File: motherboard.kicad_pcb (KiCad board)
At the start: 2 copper layers, 90.2 x 95.9 mm, 94 parts, among them P1 CONN_02X08, U1 STM32F411-LQFP64, U10 74LS125, U11 74LS125, U12 74LS125, U13 74LS125, U14 PCA9517A, U15 PCA9517A, U16 74LS125, U17 74LS125, U2 STM32F411-LQFP64, U3 AP7313, U4 74LS00, U5 74LS125, U6 FM25V20A-G, U7 FM25V20A-G, U8 FM25V20A-G, U9 FM25V20A-G, Y1 32k, Y2 8M(16pF), Y3 32k, Y4 8M(16pF)

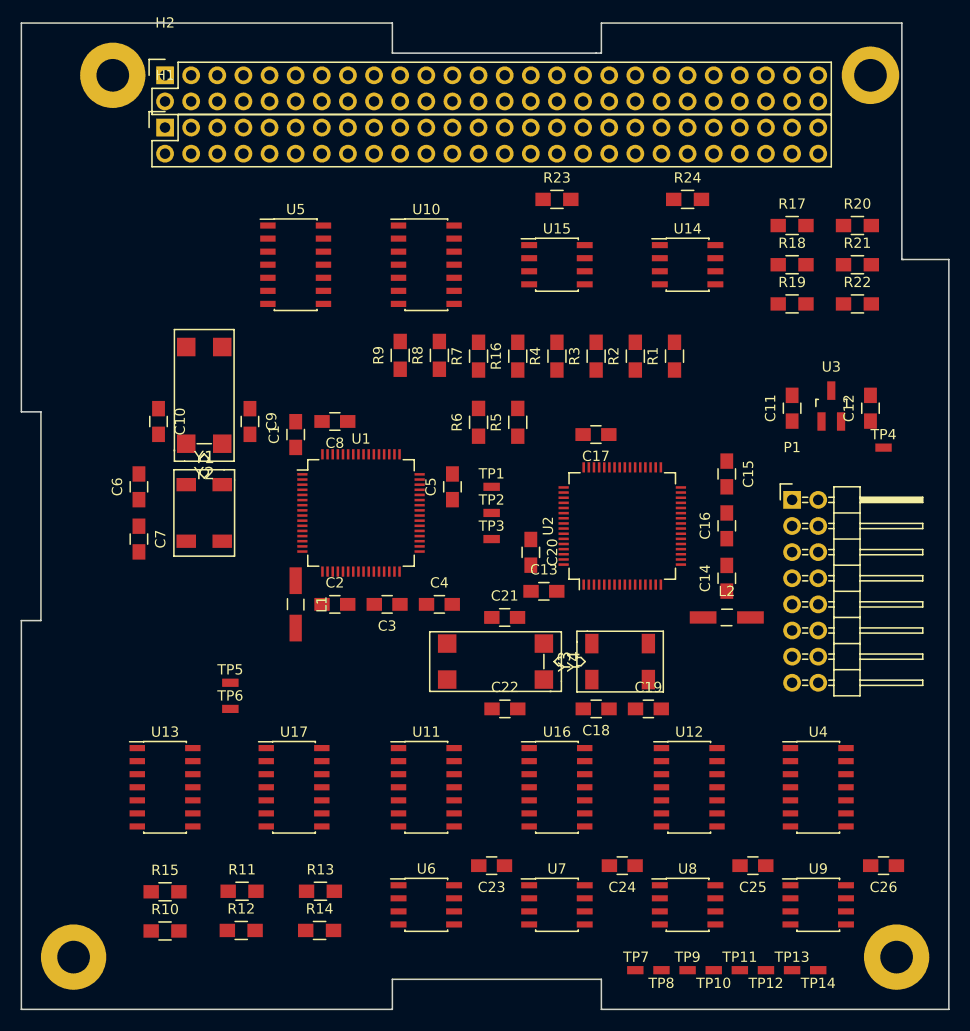
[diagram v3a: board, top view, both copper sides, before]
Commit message: Routed P1 High-speed signals
- Main UART
- Main I2C
- Mem SPI
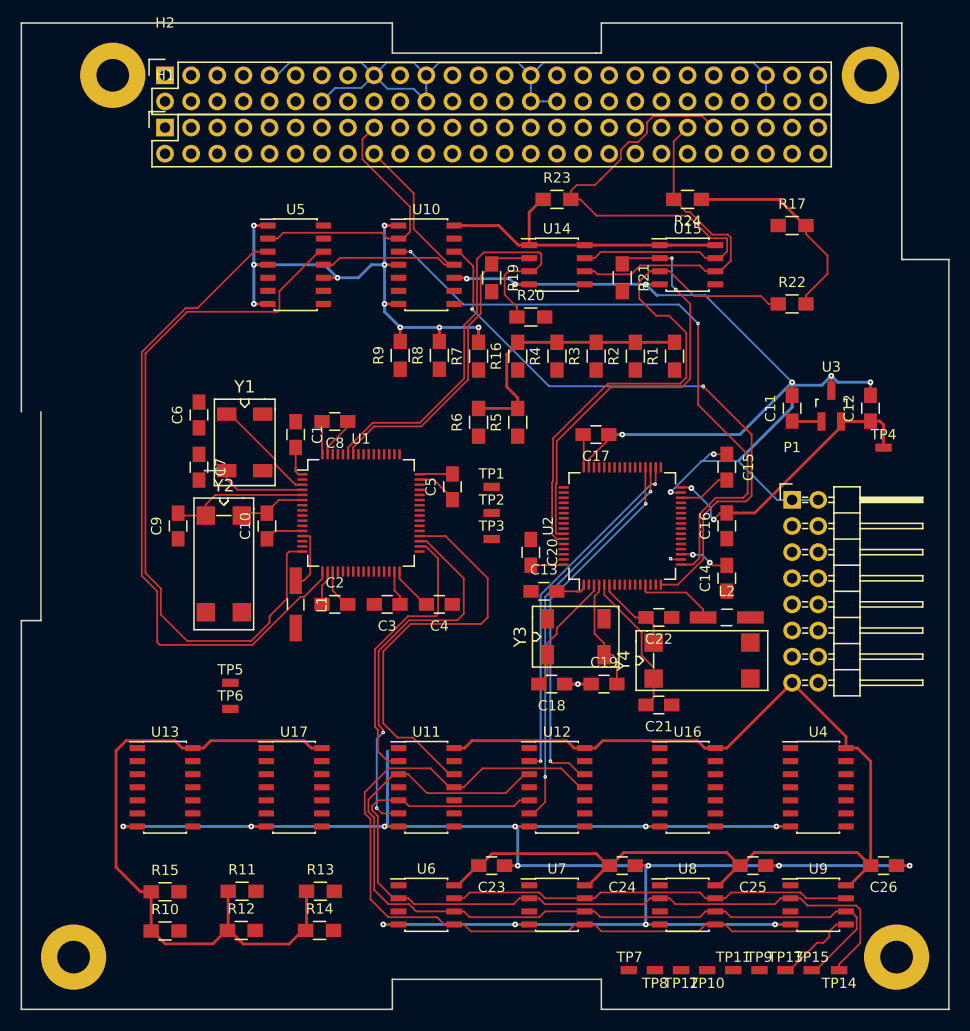
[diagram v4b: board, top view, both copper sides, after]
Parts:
- removed R18: 100K, Resistors_SMD:R_0805_HandSoldering
- added TP15: TP, motherboard:TP_0603, F.Cu at (189.9, 138.4)
- moved R20 33.0 mm to (162.6, 74.9)
- moved R19 29.3 mm to (158.8, 71.1), turned to 270 degrees
- moved R21 22.9 mm to (171.4, 71.1), turned to 270 degrees
- moved Y4 20.1 mm to (179.2, 108.3), turned to 0 degrees
- moved C22 17.4 mm to (175.0, 104.1), turned to 180 degrees
- moved C21 17.2 mm to (175.0, 112.6), turned to 180 degrees
- moved Y2 16.5 mm to (132.7, 98.9), turned to 270 degrees
- moved C10 14.6 mm to (136.9, 95.2), turned to 90 degrees
- moved U12 12.9 mm to (165.1, 120.7)
- moved U14 12.7 mm to (165.1, 69.8)
- moved U15 12.7 mm to (177.8, 69.8)
- moved U16 12.7 mm to (177.8, 120.7)
- moved C9 12.3 mm to (128.3, 95.2), turned to 90 degrees
- moved C6 9.11 mm to (130.3, 84.5)
- moved C7 9.11 mm to (130.3, 89.5)
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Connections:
- R15 pad 2: Net-(R15-Pad2) -> /MEM_NHOLD
- U11 pad 1: GND -> /NBUFEN_PRI
- U11 pad 11: /SYS_RESET -> /MEM_MOSI
- U11 pad 12: /SYS_RESET_P -> /MEM_MOSI_P
- U11 pad 2: /MEM_MISO -> /MEM_SCK_P
- U11 pad 3: /MEM_MISO_P -> /MEM_SCK
- U11 pad 4: /NBUFEN_PRI -> GND
- U11 pad 5: /MEM_SCK_P -> /MEM_MISO
- U11 pad 6: /MEM_SCK -> /MEM_MISO_P
- U11 pad 8: /MEM_MOSI -> /SYS_RESET
- U11 pad 9: /MEM_MOSI_P -> /SYS_RESET_P
- U12 pad 1: GND -> /NBUFEN_SEC
- U12 pad 11: /SYS_RESET -> /MEM_MOSI
- U12 pad 12: /SYS_RESET_S -> /MEM_MOSI_S
- U12 pad 2: /MEM_MISO -> /MEM_SCK_S
- U12 pad 3: /MEM_MISO_S -> /MEM_SCK
- U12 pad 4: /NBUFEN_SEC -> GND
- U12 pad 5: /MEM_SCK_S -> /MEM_MISO
- U12 pad 6: /MEM_SCK -> /MEM_MISO_S
- U12 pad 8: /MEM_MOSI -> /SYS_RESET
- U12 pad 9: /MEM_MOSI_S -> /SYS_RESET_S
- U6 pad 7: Net-(R15-Pad2) -> /MEM_NHOLD
- U7 pad 7: Net-(R15-Pad2) -> /MEM_NHOLD
- U8 pad 7: Net-(R15-Pad2) -> /MEM_NHOLD
- U9 pad 7: Net-(R15-Pad2) -> /MEM_NHOLD
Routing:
- net GND: track 0.00 -> 433.9 mm, vias 0 -> 35
- net +3V3: track 0.00 -> 275.9 mm
- net /MEM_MOSI: track 0.00 -> 91.1 mm
- net /MEM_SCK: track 0.00 -> 83.8 mm
- net /MEM_MISO: track 0.00 -> 79.8 mm
- net /RADIO_TX_P: track 0.00 -> 69.8 mm
- net /RADIO_RX_P: track 0.00 -> 64.7 mm
- net /RADIO_RX_S: track 0.00 -> 62.4 mm, vias 0 -> 2
- net /RADIO_TX_S: track 0.00 -> 60.0 mm, vias 0 -> 2
- net /SYS_SDA_S: track 0.00 -> 53.7 mm
- net /SYS_SCL: track 0.00 -> 52.1 mm
- net /SYS_SDA_P: track 0.00 -> 43.0 mm
- net /VDD_S: track 0.00 -> 43.0 mm, vias 0 -> 4
- net /SYS_SCL_S: track 0.00 -> 42.8 mm, vias 0 -> 2
- net /MEM_NHOLD: track 0.00 -> 40.5 mm
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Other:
- outline, holes or cut-outs redrawn
- net class Power: clearance 0.2286 -> 0.2794; trace_width 0.2286 -> 0.2794; via_dia 0.508 -> 0.5588

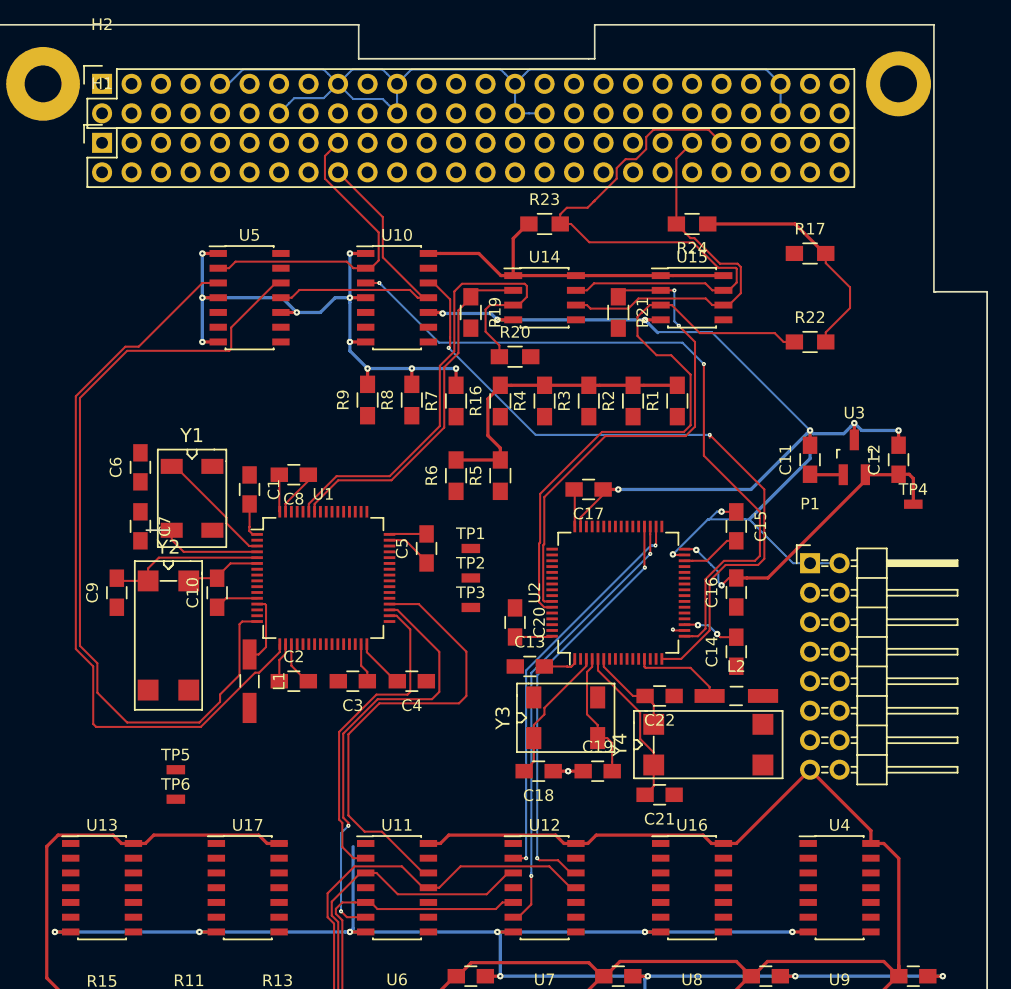
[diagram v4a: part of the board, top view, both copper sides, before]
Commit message: Much more routing completed.
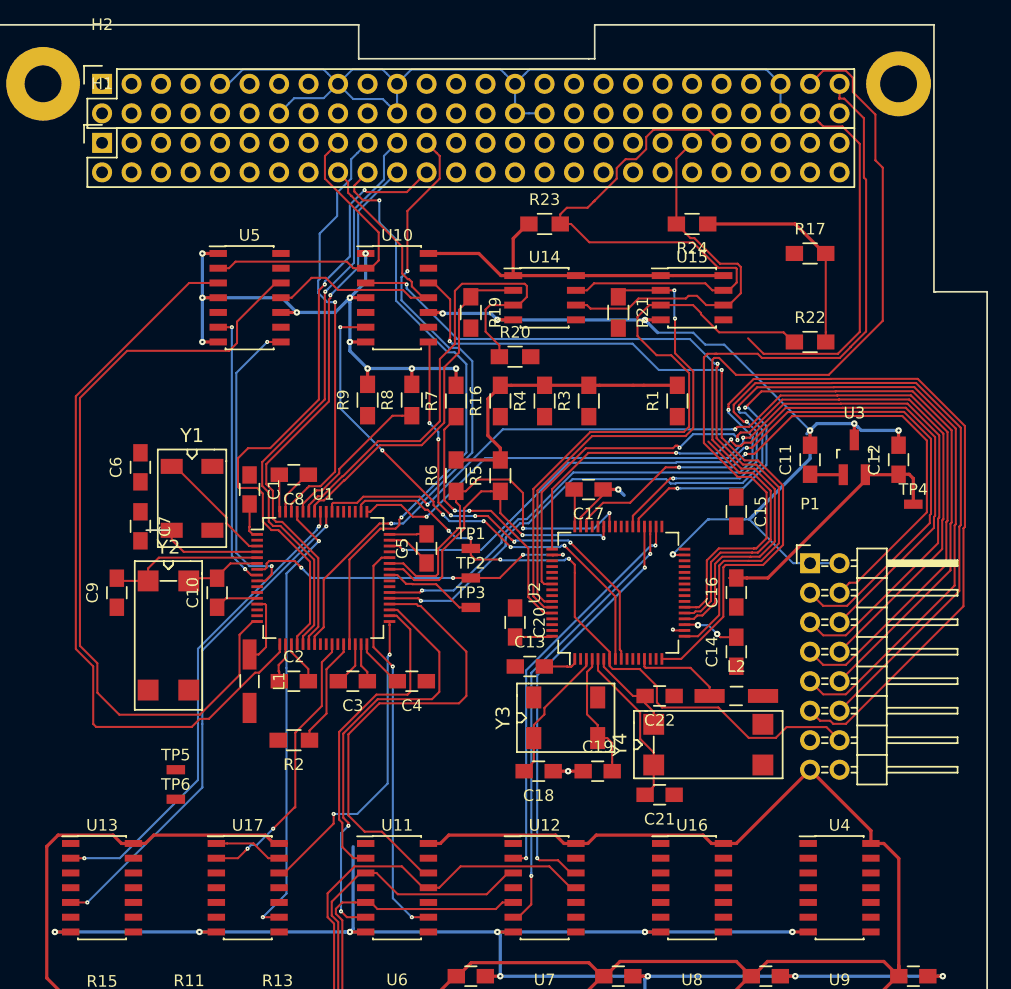
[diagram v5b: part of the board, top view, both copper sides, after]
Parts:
- moved R2 41.3 mm to (143.5, 108.0), turned to 180 degrees
- moved C15 1.27 mm to (181.6, 88.3)
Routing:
- net /UART2_RX: track 0.00 -> 98.4 mm, vias 0 -> 2
- net /UART2_TX: track 0.00 -> 95.1 mm, vias 0 -> 2
- net /SWO_P: track 0.00 -> 86.6 mm, vias 0 -> 2
- net /TCK_P: track 0.00 -> 79.5 mm, vias 0 -> 2
- net /SPI2_NSS: track 0.00 -> 74.7 mm
- net /TMS_P: track 0.00 -> 73.7 mm, vias 0 -> 2
- net /SWO_S: track 0.00 -> 71.2 mm, vias 0 -> 2
- net /UART3_RX: track 0.00 -> 70.0 mm, vias 0 -> 2
- net /SPI2_MISO: track 0.00 -> 67.9 mm
- net /UART3_TX: track 0.00 -> 64.8 mm, vias 0 -> 2
- net /TCK_S: track 0.00 -> 62.0 mm, vias 0 -> 2
- net /NRST_S: track 0.00 -> 56.4 mm, vias 0 -> 4
- net /SPI2_SCK: track 0.00 -> 55.9 mm
- net /SYS_SPI_NSS: track 0.00 -> 55.1 mm, vias 0 -> 2
- net /SYS_SPI_MOSI: track 0.00 -> 54.8 mm, vias 0 -> 2
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
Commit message: More routing
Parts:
- moved L1 0.63 mm to (139.1, 102.9)
- moved C2 0.38 mm to (143.1, 102.9)
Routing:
- net /NBUFEN_SEC: track 0.45 -> 119.3 mm, vias 0 -> 10
- net /MEM_NWP: track 0.18 -> 107.7 mm, vias 0 -> 10
- net /NBUFEN_PRI: track 5.93 -> 101.9 mm, vias 0 -> 14
- net /I2C3_SDA: track 0.00 -> 87.7 mm, vias 0 -> 2
- net /NRST_P: track 29.4 -> 112.3 mm, vias 4 -> 7
- net /I2C3_SCL: track 0.00 -> 78.7 mm, vias 0 -> 4
- net /MEM_CS0: track 0.00 -> 69.7 mm, vias 0 -> 8
- net /MEM_CS3: track 0.00 -> 66.0 mm, vias 0 -> 6
- net /SPI2_MOSI: track 0.00 -> 64.9 mm
- net /MEM_NHOLD_S: track 0.00 -> 62.4 mm, vias 0 -> 6
- net /MEM_NWP_S: track 0.00 -> 60.3 mm, vias 0 -> 6
- net /MEM_CS2: track 0.00 -> 58.3 mm, vias 0 -> 6
- net /MEM_NHOLD: track 40.5 -> 94.5 mm, vias 0 -> 8
- net /NYIELD_P: track 8.16 -> 60.2 mm, vias 0 -> 4
- net /MEM_CS1_S: track 0.00 -> 45.0 mm, vias 0 -> 2
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
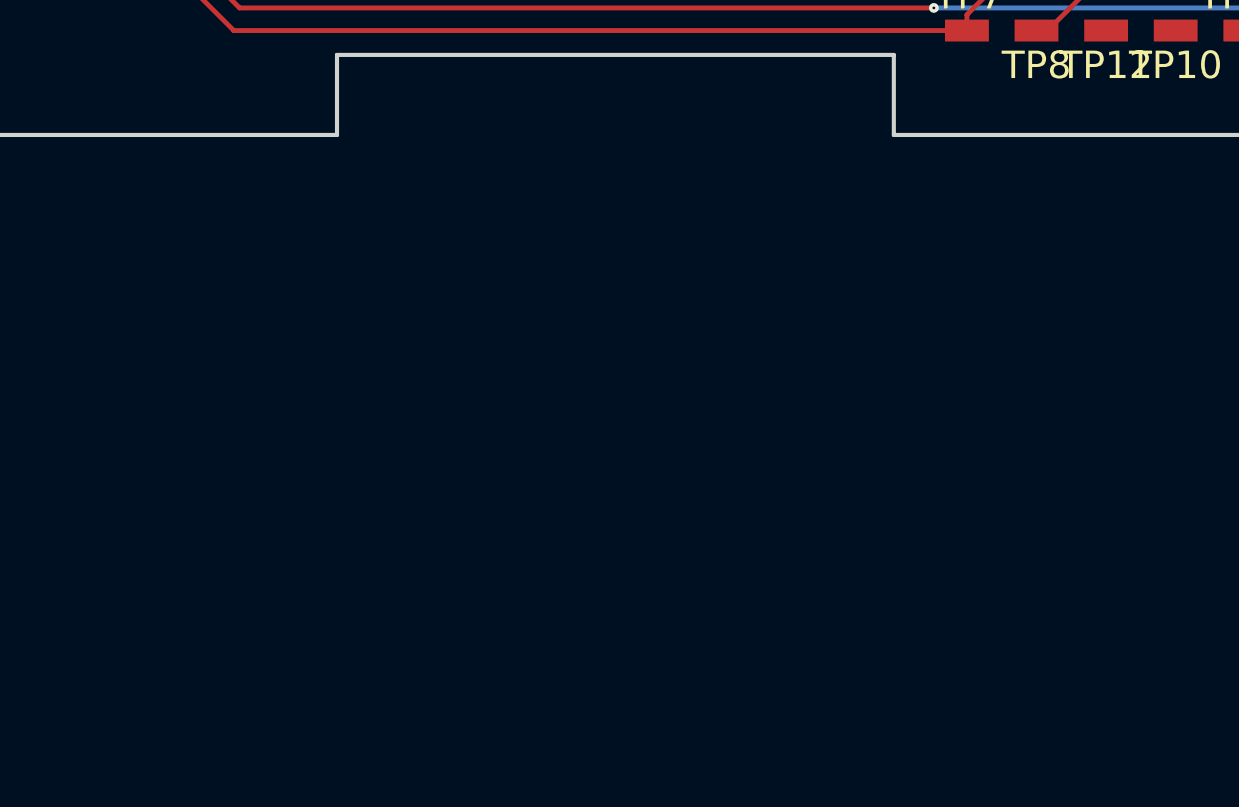
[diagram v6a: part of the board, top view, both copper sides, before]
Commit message: Began placing new components
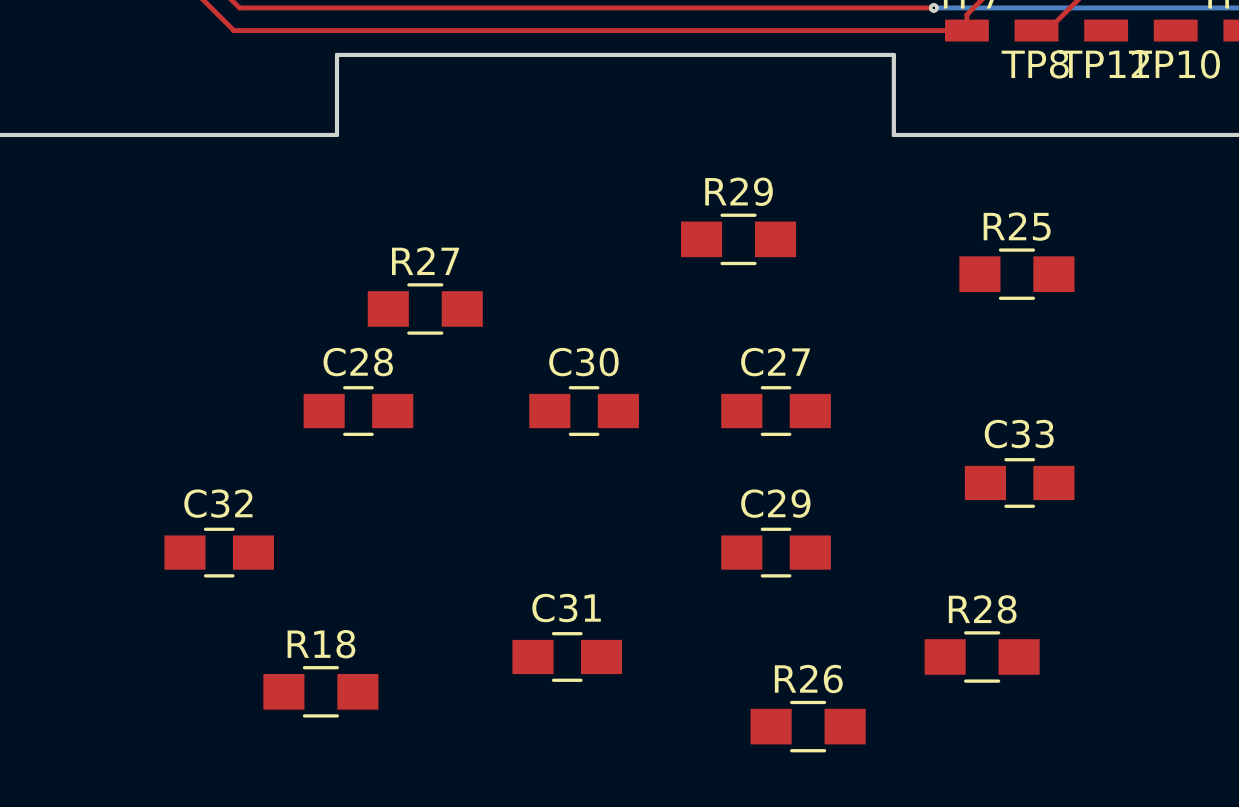
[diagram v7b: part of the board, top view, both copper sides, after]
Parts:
- added C27: 1uF, Capacitors_SMD:C_0805_HandSoldering, F.Cu at (165.1, 152.3)
- added C28: 1uF, Capacitors_SMD:C_0805_HandSoldering, F.Cu at (149.9, 152.3)
- added C29: 0.1uF, Capacitors_SMD:C_0805_HandSoldering, F.Cu at (165.1, 157.5)
- added C30: 0.1uF, Capacitors_SMD:C_0805_HandSoldering, F.Cu at (158.1, 152.3)
- added C31: 0.1uF, Capacitors_SMD:C_0805_HandSoldering, F.Cu at (157.5, 161.3)
- added C32: 0.1uF, Capacitors_SMD:C_0805_HandSoldering, F.Cu at (144.8, 157.5)
- added C33: 0.1uF, Capacitors_SMD:C_0805_HandSoldering, F.Cu at (174.0, 154.9)
- added R18: 100K, Resistors_SMD:R_0805_HandSoldering, F.Cu at (148.5, 162.6)
- added R25: 100K, Resistors_SMD:R_0805_HandSoldering, F.Cu at (173.9, 147.3)
- added R26: 100K, Resistors_SMD:R_0805_HandSoldering, F.Cu at (166.3, 163.8)
- added R27: 100K, Resistors_SMD:R_0805_HandSoldering, F.Cu at (152.3, 148.6)
- added R28: 100K, Resistors_SMD:R_0805_HandSoldering, F.Cu at (172.6, 161.3)
- added R29: 100K, Resistors_SMD:R_0805_HandSoldering, F.Cu at (163.8, 146.1)
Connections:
- H1 pad 1: /GPIO0 -> /I2C2_SCL
- H1 pad 10: /GPIO7 -> Net-(H1-Pad10)
- H1 pad 11: /GPIO8 -> /SYS_SDA
- H1 pad 12: /GPIO9 -> Net-(H1-Pad12)
- H1 pad 13: /GPIO10 -> /SGPIO13
- H1 pad 14: /GPIO11 -> Net-(H1-Pad14)
- H1 pad 15: /GPIO12 -> /SGPIO11
- H1 pad 16: /GPIO13 -> /SGPIO12
- H1 pad 17: /RADIO_RX -> /SGPIO9
- H1 pad 18: /RADIO_TX -> /SGPIO10
- H1 pad 19: /I2C2_SDA -> /SGPIO7
- H1 pad 2: /GPIO1 -> /SGPIO6
- H1 pad 20: /I2C2_SCL -> /SGPIO8
- H1 pad 21: /SYS_SPI_SCK -> Net-(H1-Pad21)
- H1 pad 22: /SYS_SPI_MISO -> Net-(H1-Pad22)
- H1 pad 23: /SYS_SPI_MOSI -> /SYS_RESET
- H1 pad 24: /SYS_SPI_NSS -> Net-(H1-Pad24)
- H1 pad 29: /SYS_RESET -> /SYS_SPI_MOSI
- H1 pad 3: /GPIO2 -> /I2C2_SDA
- H1 pad 30: Net-(H1-Pad30) -> /SYS_SPI_NSS
- H1 pad 31: Net-(H1-Pad31) -> /SYS_SPI_SCK
- H1 pad 32: Net-(H1-Pad32) -> /SYS_SPI_MISO
- H1 pad 33: /SGPIO7 -> /I2C2_SDA
- H1 pad 34: /SGPIO8 -> /I2C2_SCL
- H1 pad 35: /SGPIO9 -> /RADIO_RX
- H1 pad 36: /SGPIO10 -> /RADIO_TX
- H1 pad 37: /SGPIO11 -> /GPIO12
- H1 pad 38: /SGPIO12 -> Net-(H1-Pad38)
- H1 pad 39: /SGPIO13 -> /GPIO10
- H1 pad 4: /GPIO3 -> /SGPIO5
- H1 pad 40: /SGPIO14 -> /GPIO11
- H1 pad 41: /SYS_SDA -> /GPIO8
- H1 pad 42: Net-(H1-Pad42) -> /GPIO9
- H1 pad 43: /SYS_SCL -> /GPIO6
- H1 pad 44: Net-(H1-Pad44) -> /GPIO7
- H1 pad 45: Net-(H1-Pad45) -> /GPIO4
- H1 pad 46: Net-(H1-Pad46) -> /GPIO5
- H1 pad 47: /NBUFEN_PRI -> /RADIO_TR
- H1 pad 48: /NBUFEN_SEC -> /RADIO_RR
- H1 pad 49: /I2C2_SDA -> /GPIO2
- H1 pad 5: /RADIO_TR -> /NBUFEN_PRI
- H1 pad 50: /SGPIO5 -> /GPIO3
- H1 pad 51: /I2C2_SCL -> /GPIO0
- H1 pad 52: /SGPIO6 -> /GPIO1
- H1 pad 6: /RADIO_RR -> /NBUFEN_SEC
- H1 pad 7: /GPIO4 -> Net-(H1-Pad7)
- H1 pad 8: /GPIO5 -> Net-(H1-Pad8)
- H1 pad 9: /GPIO6 -> /SYS_SCL
- U1 pad 50: /NRST_S -> /NRST1_S
- U1 pad 54: /GPIO13 -> /NRST2_S
- U2 pad 2: /SGPIO13 -> /GPIO13
- U2 pad 50: /NRST_P -> /NRST1_P
- U2 pad 54: /SGPIO14 -> /NRST2_P
- U4 pad 10: (no net) -> /NRST2_P
- U4 pad 11: (no net) -> /NRST_S
- U4 pad 12: (no net) -> /NRST1_S
- U4 pad 13: (no net) -> /NRST2_S
- U4 pad 8: (no net) -> /NRST_P
- U4 pad 9: (no net) -> /NRST1_P
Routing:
- net /SGPIO8: track 0.00 -> 38.3 mm, vias 0 -> 2
- net /I2C2_SCL: track 51.6 -> 13.3 mm, vias 2 -> 0
- net Net-(H1-Pad22): track 0.00 -> 32.3 mm, vias 0 -> 1
- net /SYS_SPI_MISO: track 50.2 -> 17.9 mm, vias 1 -> 0
- net Net-(H1-Pad24): track 0.00 -> 25.8 mm, vias 0 -> 2
- net /SYS_SPI_NSS: track 57.6 -> 31.8 mm, vias 2 -> 0
- net /RADIO_RR: track 21.9 -> 3.16 mm, vias 4 -> 1
- net /NBUFEN_SEC: track 119.3 -> 138.0 mm, vias 10 -> 13
- net /SGPIO7: track 0.00 -> 16.5 mm
- net /I2C2_SDA: track 36.7 -> 20.2 mm
- net /SYS_SCL: track 52.1 -> 36.0 mm
- net /GPIO6: track 0.00 -> 16.1 mm
- net Net-(H1-Pad21): track 0.00 -> 15.4 mm, vias 0 -> 1
- net /SYS_SPI_SCK: track 53.0 -> 37.6 mm, vias 1 -> 0
- net /SYS_SPI_MOSI: track 59.0 -> 44.9 mm, vias 2 -> 1
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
